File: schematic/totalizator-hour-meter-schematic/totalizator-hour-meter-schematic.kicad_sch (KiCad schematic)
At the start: 3 parts, among them J1 Analog, J2 Digital, U1 ESP32-C3-DevKitM-1

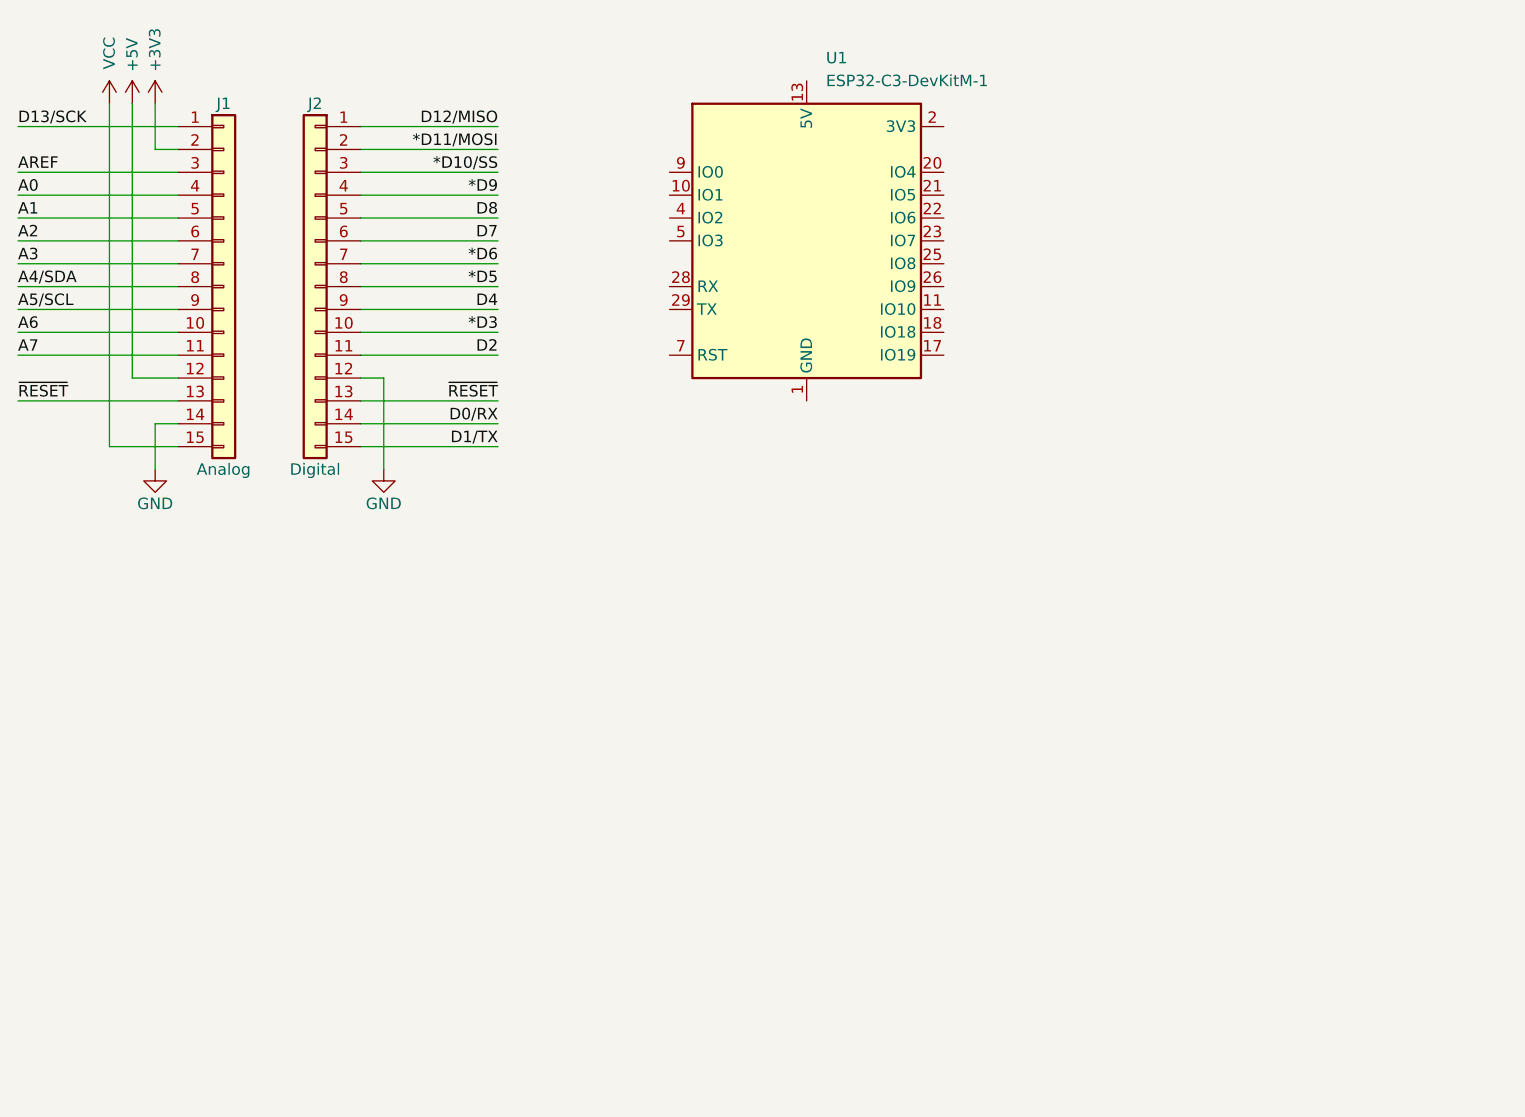
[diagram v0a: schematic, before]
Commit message: feat(simulator): add Drive mode with vehicles on a map and IMU-only dead reckoning
- /drive: a truck, plane or uploaded glTF model drives on OpenStreetMap tiles
  (MapLibre + three.js), by drawn route, live keyboard/gamepad (remappable)
  or GPX/CSV replay
- vehicle motion becomes IMU data (specific force, body rates, earth field,
  vibration) and runs through a port of the firmware's IMU pipeline, so
  reported roll/pitch/heading carry the device's real errors in turns
- reference host-side estimators fed with the frames the host receives:
  ground vehicles learn gravity while parked with zero-velocity updates;
  aircraft use a 3D strapdown INS; truth vs estimate drawn with the error
- CLI: --drive truck|plane, --origin lat,lon, --route file.gpx|.csv, --loop
- auto IMU values follow the attitude; vehicle as a third input source
- sample route around Merdeka Square from OpenStreetMap road geometry
- bench pitch follows the firmware's sign (positive = nose down)
- bump simulator to 1.2.0
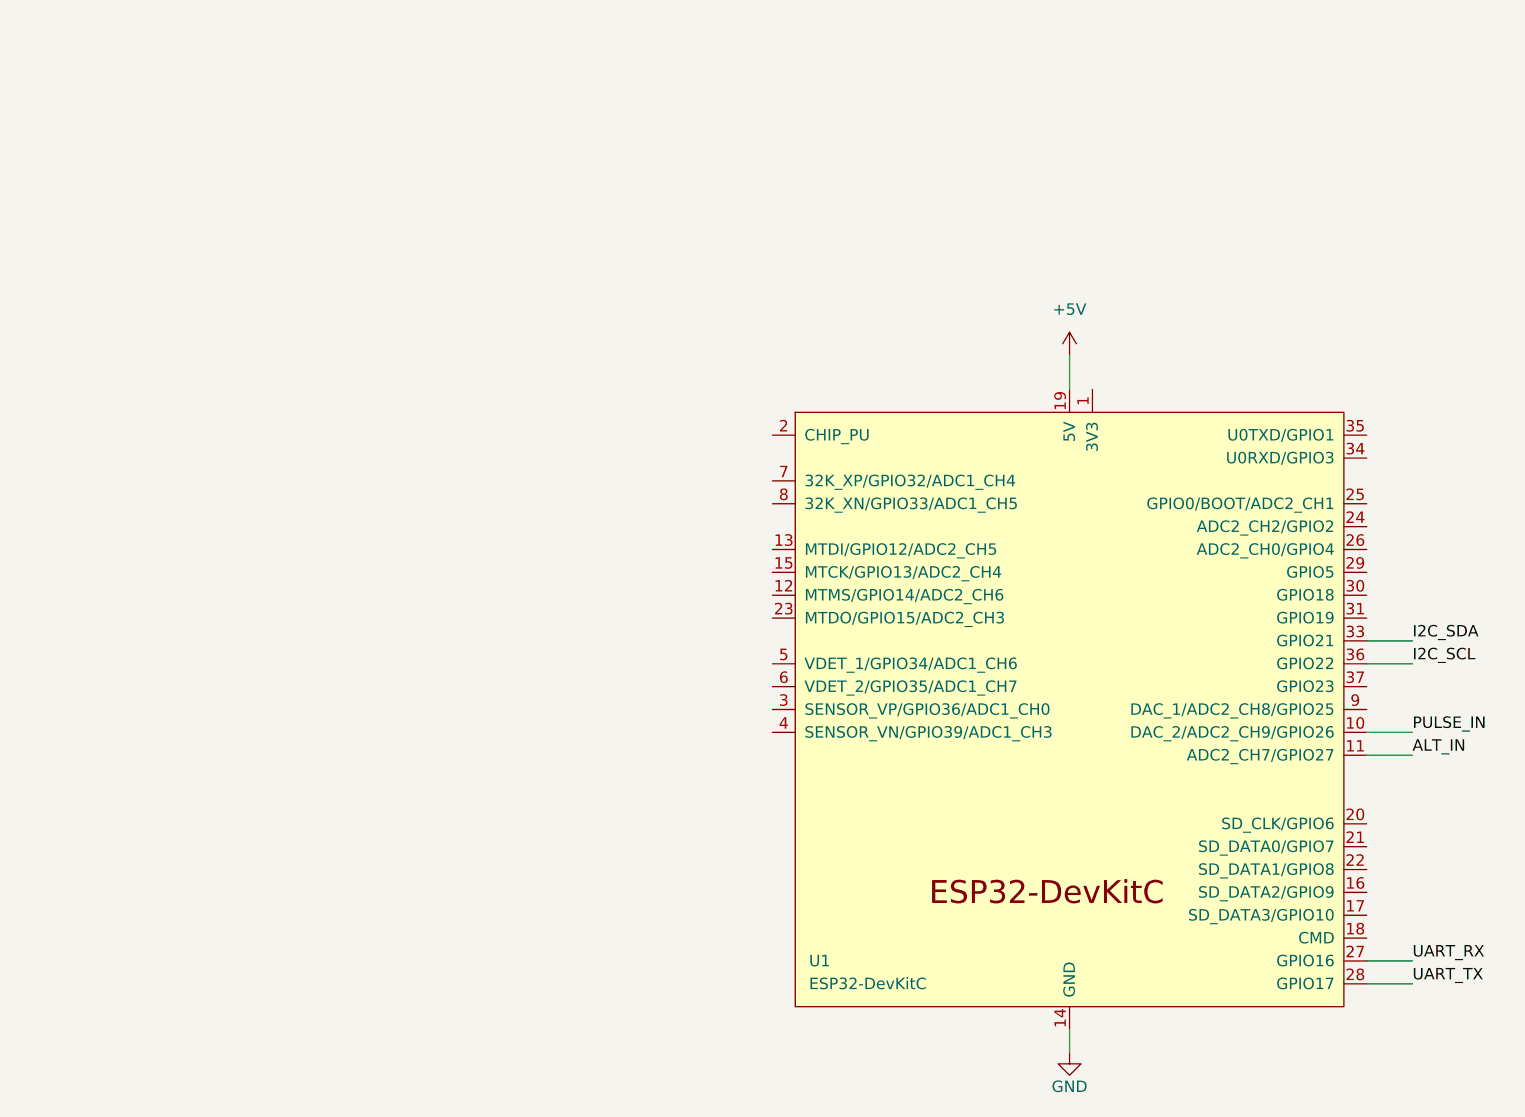
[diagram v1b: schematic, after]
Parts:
- removed J1: Analog, Connector_PinHeader_2.54mm:PinHeader_1x15_P2.54mm_Vertical, symbol Connector_Generic:Conn_01x15
- removed J2: Digital, Connector_PinHeader_2.54mm:PinHeader_1x15_P2.54mm_Vertical, symbol Connector_Generic:Conn_01x15
- removed U1: ESP32-C3-DevKitM-1, RF_Module:ESP32-C3-DevKitM-1, symbol RF_Module:ESP32-C3-DevKitM-1
- added U1: ESP32-DevKitC, PCM_Espressif:ESP32-DevKitC, symbol PCM_Espressif:ESP32-DevKitC
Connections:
- net +5V: now also U1.19 (5V)
- net GND: now also U1.14 (GND), U1.32 (GND), U1.38 (GND)
- new net ALT_IN: U1.11 (ADC2_CH7/GPIO27)
- new net I2C_SCL: U1.36 (GPIO22)
- new net I2C_SDA: U1.33 (GPIO21)
- new net PULSE_IN: U1.10 (DAC_2/ADC2_CH9/GPIO26)
- new net UART_RX: U1.27 (GPIO16)
- new net UART_TX: U1.28 (GPIO17)
